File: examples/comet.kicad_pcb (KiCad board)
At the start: 2 copper layers, 17.8 x 33 mm, 24 parts, among them J1 USB-C, J2 01x02, J3 01x12, J4 01x12, J5 01x05, U1 ATmega32U4, X1 16MHz

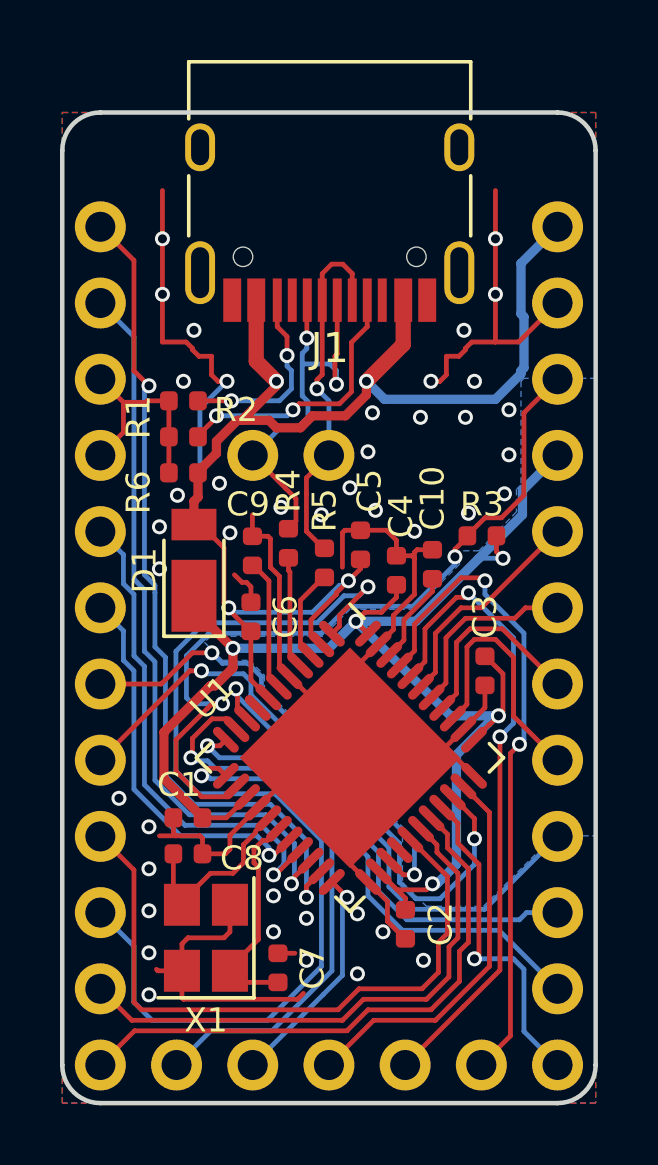
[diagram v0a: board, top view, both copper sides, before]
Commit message: Add bzlmod support
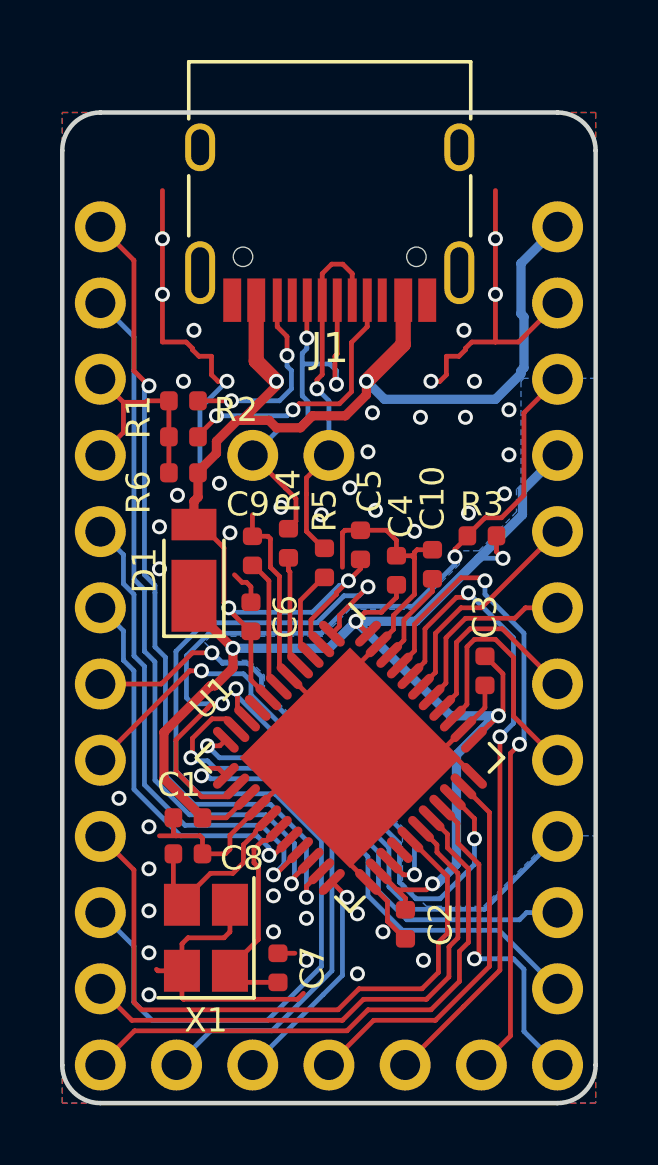
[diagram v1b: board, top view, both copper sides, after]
